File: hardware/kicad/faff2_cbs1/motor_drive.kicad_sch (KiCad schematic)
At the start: 77 parts, among them J1101 1x6 2.54mm, J1102 1x6 2.54mm, J1103 Micro-Fit 1x3, Q1101 BSZ099N06LS5, Q1102 BSZ099N06LS5, Q1103 BSZ099N06LS5, Q1104 BSZ099N06LS5, Q1105 BSZ099N06LS5, Q1106 BSZ099N06LS5, U1101 DRV8323S

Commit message: review r1 batch 3: motor_drive - bridge decoupling, label flow, R1101/R1102 note
The captain's motor_drive batch, all four points.

  1  the 24 V feed note said R101/R102 and read as fit-one-or-the-other. The
     refdes were wrong; the parts are genuinely two 0R in series, both fitted
     (D-MOT-14), so the note is rewritten to say that outright and give each
     link its own job
  2  C1101's reference ran into C1102's body at the old 8.89 pitch - the bulk
     column respaced, and TP1103 moved clear of the capacitor value row
  3  eight hierarchical labels had their text lying along their own wire:
     seven took their wire from the left while facing left, and +24V_SW ran
     vertically into the block title. All now face the way their wire arrives,
     in one aligned column
  4  one 2.2 uF + 100 nF pair added per half-bridge (C1119..C1124)

On point 4: the sheet already had DC-link bulk (210 uF at the bus entry) and the
gate driver's own VM bypass, but nothing at all in the power-stage block. TI asks
for exactly this in SLVSDJ3D 10 and 11.1 - additional capacitance bypassing the
external half-bridge MOSFETs, placed to minimise the high-current path through
them. Sized from the sheet's own operating point: 1.9 A at 20 kHz over a ~100 ns
edge is ~190 nC, so 0.4 V of sag wants ~0.5 uF; 2.2 uF 100 V gives 4x margin and
barely derates at 24 V, and the 100 nF 0805 has the lower ESL for the edge.

Per FET is not done and should not be: a capacitor across one MOSFET is a
snubber, not decoupling - it needs a series resistor sized against measured
ringing, and it is a bring-up decision, not a default.

ERC 0 errors / 0 warnings at severity-all. 398 -> 404 components, 251 nets
unchanged; the only nets that move are V24_MOT and GND, each gaining the six new
capacitor pins - every other node set is identical to main. motor_drive is clean
under the overlap checker.

The first cap placement put stubs collinear with the DRV's gate fan-out verticals
and shorted two gate nets 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
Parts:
- added C1119, C1121, C1123: 2.2uF, Amodo:C_1206_3216Metric, symbol Amodo_Capacitors:CAP_MLCC_2.2uF_1206_10%_100V
- added C1120, C1122, C1124: 100nF, Amodo:C_0805_2012Metric, symbol Amodo_Capacitors:CAP_MLCC_100nF_0805_10%_100V
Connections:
- net GND: now also C1119.2, C1120.2, C1121.2, C1122.2, C1123.2, C1124.2
- net V24_MOT: now also C1119.1, C1120.1, C1121.1, C1122.1, C1123.1, C1124.1
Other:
- note added: "BRIDGE DECOUPLING one 2.2 uF + 100 nF pair per half-bridge: C1119/C1120 phase U, C1121/C1122 phase V, C1123/C1124 phase W. The 210 uF bulk at the bus entry is too far round the loop to serve commutation; each pair goes hard against its own leg, across the high-side drain and the shunt return. Not per FET - a capacitor across one FET is a snubber, not decoupling, and is a bring-up decision (SLVSDJ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"
- note added: "R1101 and R1102 are in SERIES and both fitted - two 0R links, not alternatives to each other. R1101 is the isolation link: open it and the logic side stays powered, actuator dead (TEST_PLAN 3.3). R1102 is the current-measurement break: lift it and fit a shunt to read the motor bus current."
- note removed: "R101 isolation link, R102 current-measurement break. Both fitted. Opening R101 leaves the whole logic side powered with the actuator dead - TEST_PLAN.md 3.3, step 8."
- moved on the sheet: C1102, C1103, C1104, TP1103

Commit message: review r1 final sweep: power labels, TP silkscreen names, text overlaps
The captain's design-wide pass, run once the per-sheet batches had landed.
Presentation only: ERC 0 errors / 0 warnings at severity-all, 404 components,
251 nets, and every per-net node set identical to the pre-sweep export.

  power labels   92 rail names were hidden on loadcell_afe, motor_drive and
                 temp_sense - all 285 power symbols now read, placed to the
                 house pattern (GND below the symbol, rail arrows above)
  test points    66 of 83 still carried the library default "TestPoint". All
                 83 now name what they measure, from the net they actually
                 land on in the netlist; longest is 5 characters
  text overlap   16 collisions cleared design-wide, four of them sub-millimetre
                 ones the bundled checker passes because it under-measures text
  GND upside down  none - 0 of 285 power symbols is rotated or mirrored
  graphic/wire   one: power_rails block D's bottom border lay along the last
                 PWR_FLAG's wire; the flag column moved up 2.54

The overlap checker turns out to have three separable blind spots, each settled
here by measuring a render rather than by reading the format: it grows every
text field rightward regardless of justify/mirror/180-rotation, so its box is a
mirror image of the truth for those and it both invents and misses collisions;
it measures text at ~1.06 mm per character where the real advance is ~1.19; and
it reflects a rotated symbol's body about the origin. tools/sch_geom.py models
all three correctly and the design is clean under it design-wide. Two of that
model's own rules - notes growing up from their anchor, and labels taking no
180-degree justify flip - were bugs of mine that the checker caught first. The
render is what settles it; neither tool is authoritative alone.

Placement is searched rather than guessed: 177 newly visible fields are tried
against every wire, block border, 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
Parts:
- TP1101, TP1102: value TestPoint -> 24MOT
- TP1103: value TestPoint -> VBUSM
- TP1104: value TestPoint -> FETT
- TP1105: value TestPoint -> VENC
- TP1106: value TestPoint -> VMDRV
- TP1107: value TestPoint -> VCP
- TP1108: value TestPoint -> GND
- TP1109: value TestPoint -> nFLT
- TP1110: value TestPoint -> SOA
- TP1111: value TestPoint -> SOB
- TP1112: value TestPoint -> SOC
- TP1113: value TestPoint -> GHA
- TP1114: value TestPoint -> GLA
- TP1115: value TestPoint -> PH_U
- TP1116: value TestPoint -> GHB
- TP1117: value TestPoint -> GLB
- TP1118: value TestPoint -> PH_V
- TP1119: value TestPoint -> GHC
- TP1120: value TestPoint -> GLC
- TP1121: value TestPoint -> PH_W

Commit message: review r2 item 3: answer D601/D602, and close the one real ESD gap
D602 is NOT per-connector ESD. It is a DNP second footprint in parallel with
D601 on the read head's 5 V feed, added at the captain's own request in the AFE
review round - one of three DNP parallel bring-up positions on that supply
(R608 on R601, R609 on FB601, D602 on D601), none fitted by default. J601 and
J602 carry the same ten signals in parallel for the same head, so a clamp on
either serves both.

The rest of the board follows a policy that was already written down and is
exposure-based rather than per-connector: clamps where a pin leaves the
enclosure (24 V input, USB-C, SMA) or gets hot-plugged (the FFC's supply), and
everywhere else a series resistor and an RC bounding the current into a device
that can take it. REQ-SC-01 - prototype, EMC best practice, no formal testing -
is what makes that proportionate. The full interface-by-interface audit is in
the decisions file.

The audit found one real gap. J1101/J1102, the motor encoder and hall harness,
ran connector -> pull-up -> MCU pin with nothing in between on six pins, while
the equally internal limit harness gets 1k + 100R + 10n and the buttons get
100R + 100n, both explicitly to protect the MCU pins. Two internal harnesses,
two different answers.

Added R1128..R1133, 100R in series, one per line. At the ~270 kHz D-MOT-11
sizes these for, that is free, and it bounds the fault current into six GPIOs.
No TVS array: the cable is internal and an array would load the lines for
exposure this design does not have. A pre-rotated RES_TF_100R_0603_H joins
faff2_passives.kicad_sym rather than six rotated instances.

Nothing added on J501/J701/J702: diode capacitance and leakage on a 2 mV/V
bridge and on RTD/NTC inputs is the AFE owner's call against REQ-FF-04, so it
is raised rather than taken.

ERC 0/0 at severity-all; 406 -> 412 components, 253 -> 259 nets, exactly the six
resistors and the six nets their insertion creates.

Co-Authored-By: Claude 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
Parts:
- added R1128, R1129, R1130, R1131, R1132, R1133: 100R, Amodo:R_0603_1608Metric, symbol faff2_passives:RES_TF_100R_0603_H
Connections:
- net HALL1: now also R1131.2; no longer J1102.2, R1111.2
- net HALL2: now also R1132.2; no longer J1102.3, R1112.2
- net HALL3: now also R1133.2; no longer J1102.4, R1113.2
- net MOTOR_ENCODER_A: now also R1128.2; no longer J1101.2, R1108.2
- net MOTOR_ENCODER_B: now also R1129.2; no longer J1101.3, R1109.2
- net MOTOR_ENCODER_I: now also R1130.2; no longer J1101.4, R1110.2
- new net: J1102.4, R1113.2, R1133.1
- new net: J1102.2, R1111.2, R1131.1
- new net: J1102.3, R1112.2, R1132.1
- new net: J1101.2, R1108.2, R1128.1
- new net: J1101.3, R1109.2, R1129.1
- new net: J1101.4, R1110.2, R1130.1
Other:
- note added: "J102 A/B/Z -> TIM3 CH1/CH2/CH3 (PC6/PC7/PC8). J103 halls -> PE14/PD14/PD15 (GPIO). Motor not fixed (DEC-0004): this pinout suits every candidate BLDC in the design log. R1128..R1133 100R bound the current into the six MCU pins, the same treatment the limit and button harnesses get. The cable is internal, so no TVS array - see the ESD audit in docs/decisions/actuator-sch-review-r1.md."
- note removed: "J102 A/B/Z -> TIM3 CH1/CH2/CH3 (PC6/PC7/PC8). J103 halls -> PE14/PD14/PD15 (GPIO). Motor not fixed (DEC-0004): this pinout suits every candidate BLDC in the design log."

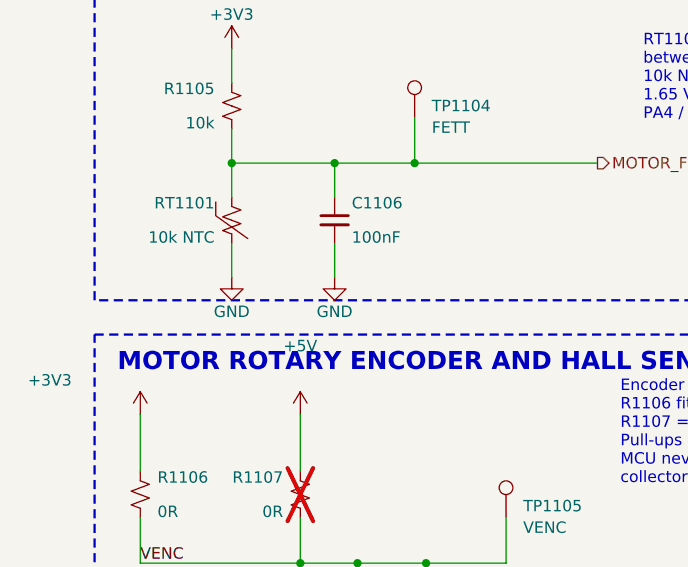
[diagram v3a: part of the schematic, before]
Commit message: review r2 items 4-7: four per-sheet placement fixes
  4  linear_encoder - U601A's GND body ended at y=166.37 and U601E's +3V3 body
     began at exactly 166.37, so the two flags were touching. The whole U601E
     group drops 7.62 - unit, both flags, four wires, and the no_connect on its
     unused output, which does NOT ride with the symbol: ERC caught that as
     pin_not_connected plus a dangling no-connect the first time round.
  5  temp_sense - C704/C705's grounds sat 0.6 mm above the REFP row with
     TP705's reference on the row itself; the caps and grounds move up 5.08.
     Three verticals ran through the block title, so it is shortened to
     "CHANNEL 2 FILTER + SHARED REF", which at size 1.778 ends at x=135.9 and
     clears the leftmost of them at 137.16.
  6  ui_io - R915's reference sat on its own body. It is the horizontal 0R
     variant but its fields were still on the vertical pattern; moved to the
     _H symbol's own pattern.
  7  motor_drive - #PWR1109/#PWR1110 bodies ended exactly on the block border
     and their GND text was outside the box entirely. Both move up to 138.43.

ERC 0 errors / 0 warnings at severity-all; 412 components, 259 nets, node sets
identical - all four are placement only.

Co-Authored-By: Claude Opus 5 <noreply@anthropic.com>
Claude-Session: https://claude.ai/code/session_01PFWfwT8RZc8Zqn8vgZxV8j
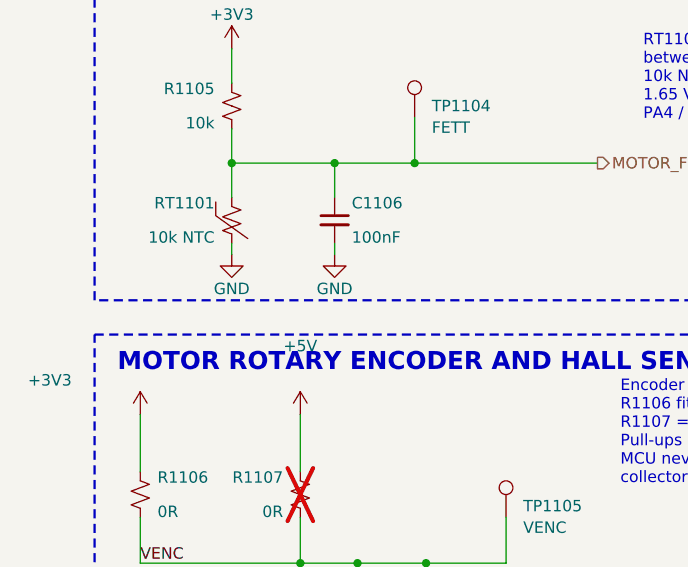
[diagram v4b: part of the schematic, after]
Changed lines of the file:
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@@
 		)
 	)
+	(wire
+		(pts
+			(xy 30.48 137.16) (xy 30.48 138.43)
+		)
+		(stroke
+			(width 0)
+			(type default)
+		)
+	)
+	(wire
+		(pts
+			(xy 41.91 137.16) (xy 41.91 138.43)
+		)
+		(stroke
+			(width 0)
+			(type default)
+		)
+	)
 	(symbol
 		(lib_id "faff2_passives:RES_TF_100R_0603_H")
@@
 	(symbol
 		(lib_id "Amodo_Symbols:GND")
-		(at 30.48 140.97 0)
+		(at 30.48 138.43 0)
 		(unit 1)
 		(exclude_from_sim no)
@@
 		(dnp no)
 		(property "Reference" "#PWR1109"
-			(at 30.48 134.62 0)
+			(at 30.48 138.43 0)
 			(effects
 				(font
@@
 		)
 		(property "Value" "GND"
-			(at 30.48 144.78 0)
+			(at 30.48 142.24 0)
 			(effects
 				(font
@@
 		)
 		(property "Footprint" ""
-			(at 30.48 140.97 0)
+			(at 30.48 138.43 0)
 			(effects
 				(font
@@
 		)
 		(property "Datasheet" ""
-			(at 30.48 140.97 0)
+			(at 30.48 138.43 0)
 			(effects
 				(font
@@
 		)
 		(property "Description" "Power symbol creates a global label with name \"GND\" , ground"
-			(at 30.48 140.97 0)
+			(at 30.48 138.43 0)
 			(effects
 				(font
@@
 	(symbol
 		(lib_id "Amodo_Symbols:GND")
-		(at 41.91 140.97 0)
+		(at 41.91 138.43 0)
 		(unit 1)
 		(exclude_from_sim no)
@@
 		(dnp no)
 		(property "Reference" "#PWR1110"
-			(at 41.91 134.62 0)
+			(at 41.91 138.43 0)
 			(effects
 				(font
@@
 		)
 		(property "Value" "GND"
-			(at 41.91 144.78 0)
+			(at 41.91 142.24 0)
 			(effects
 				(font
@@
 		)
 		(property "Footprint" ""
-			(at 41.91 140.97 0)
+			(at 41.91 138.43 0)
 			(effects
 				(font
@@
 		)
 		(property "Datasheet" ""
-			(at 41.91 140.97 0)
+			(at 41.91 138.43 0)
 			(effects
 				(font
@@
 		)
 		(property "Description" "Power symbol creates a global label with name \"GND\" , ground"
-			(at 41.91 140.97 0)
+			(at 41.91 138.43 0)
 			(effects
 				(font
@@
 	(wire
 		(pts
-			(xy 30.48 137.16) (xy 30.48 140.97)
-		)
-		(stroke
-			(width 0)
-			(type default)
-		)
-	)
-	(wire
-		(pts
 			(xy 31.75 190.5) (xy 31.75 193.04)
 		)
@@
 		)
 		(stroke
-			(width 0)
-			(type default)
-		)
-	)
-	(wire
-		(pts
-			(xy 41.91 137.16) (xy 41.91 140.97)
-		)
-		(stroke
